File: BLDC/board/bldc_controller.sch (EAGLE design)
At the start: 112 parts, among them IC1 DRV8301, IC2 OPA2374, IC3 AS 5134, IC5 TPS51103, M1 FRDM-KL05Z, M2 MBED_NXP_LPC1768, Q1 MOSFET-NCHANNELSMD, Q2 MOSFET-NCHANNELSMD, Q3 P-CHANNEL-MOSFETTO252, Q4 SLPS388A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

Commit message: Fixed encoder alignment. May still need to fix holes for BLDC motor
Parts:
- IC3: device biomimetic:AS5134 -> modular_robotics:AS5134
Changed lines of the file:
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@@
 <part name="GND32" library="biomimetic" deviceset="GND" device=""/>
 <part name="FRAME5" library="biomimetic" deviceset="FRAME-LETTER" device=""/>
-<part name="IC3" library="biomimetic" deviceset="AS5134" device="" value="AS 5134"/>
+<part name="IC3" library="modular_robotics" deviceset="AS5134" device="" value="AS 5134"/>
 <part name="C28" library="biomimetic" deviceset="CAP" device="0402-CAP" value="100nF"/>
 <part name="GND33" library="biomimetic" deviceset="GND" device=""/>

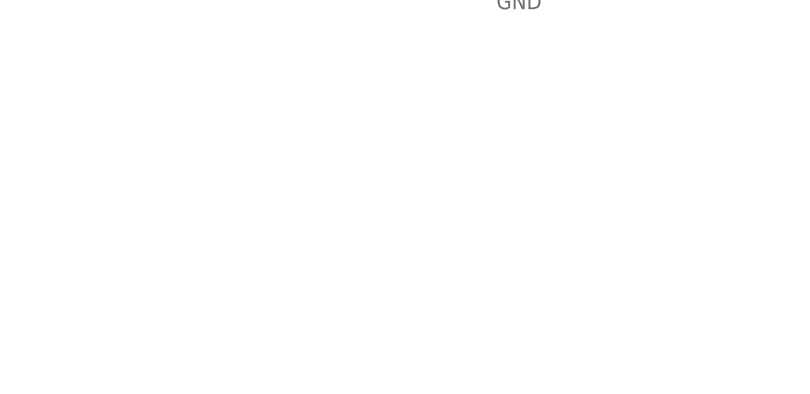
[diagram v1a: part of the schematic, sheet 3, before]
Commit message: Corrected BLDC mounting holes, added borders to boards, squeezed one more ADC board in to panelization
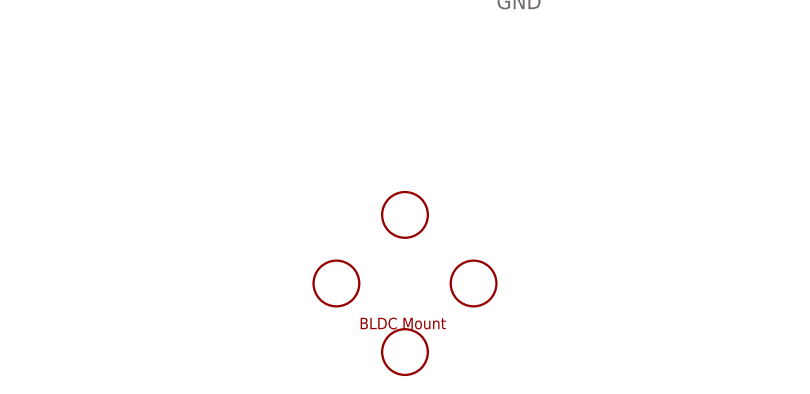
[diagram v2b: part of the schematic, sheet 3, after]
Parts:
- added U$8: BLDC_MOUNT, modular_robotics:BLDC_MOUNT
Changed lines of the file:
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@@
 <part name="ICN" library="modular_robotics" deviceset="INA199A1" device=""/>
 <part name="U$4" library="biomimetic" deviceset="5V" device=""/>
+<part name="U$8" library="modular_robotics" deviceset="BLDC_MOUNT" device=""/>
 </parts>
 <sheets>
@@
 <instance part="ICN" gate="G$1" x="134.62" y="68.58"/>
 <instance part="ICN" gate="G$2" x="137.16" y="68.58"/>
+<instance part="U$8" gate="G$1" x="121.92" y="20.32"/>
 </instances>
 <busses>
